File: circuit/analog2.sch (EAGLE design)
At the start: 44 parts, among them IC1 AD8532, IC2 74HC4052D, IC3 AD8532, IC4 4066D, IC5 4066D

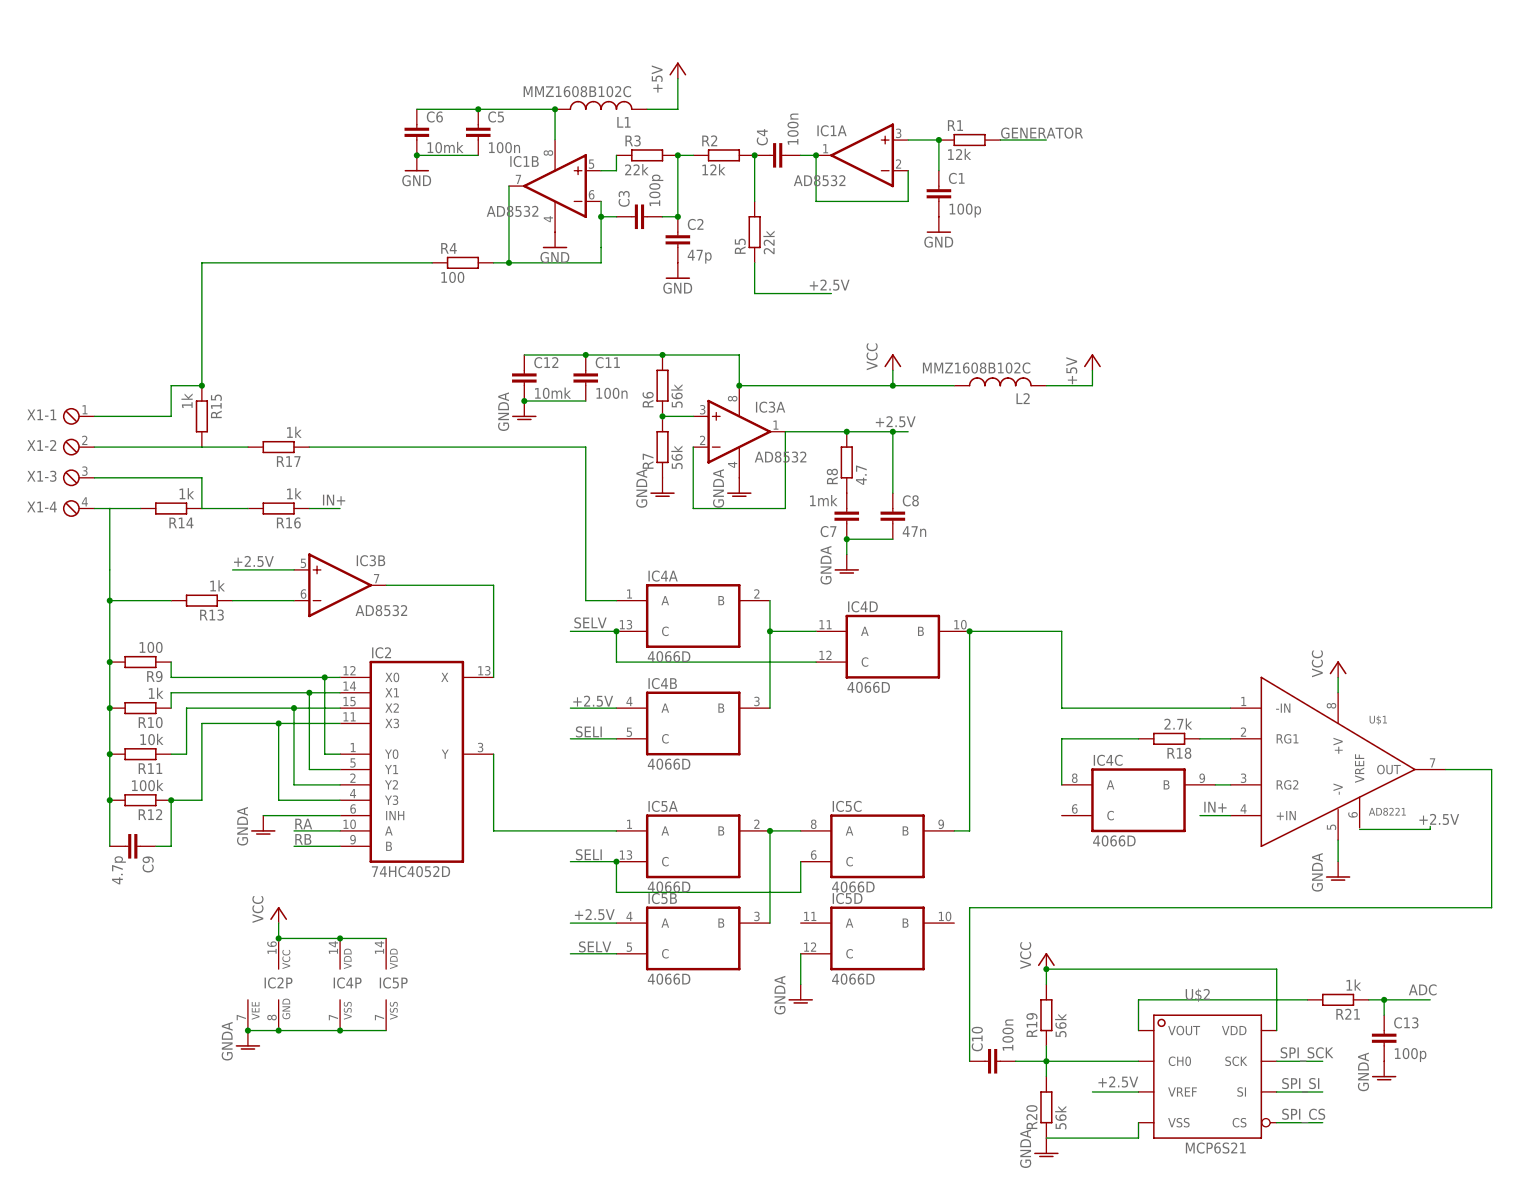
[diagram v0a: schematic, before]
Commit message: - analog to dual ADC STM32F103
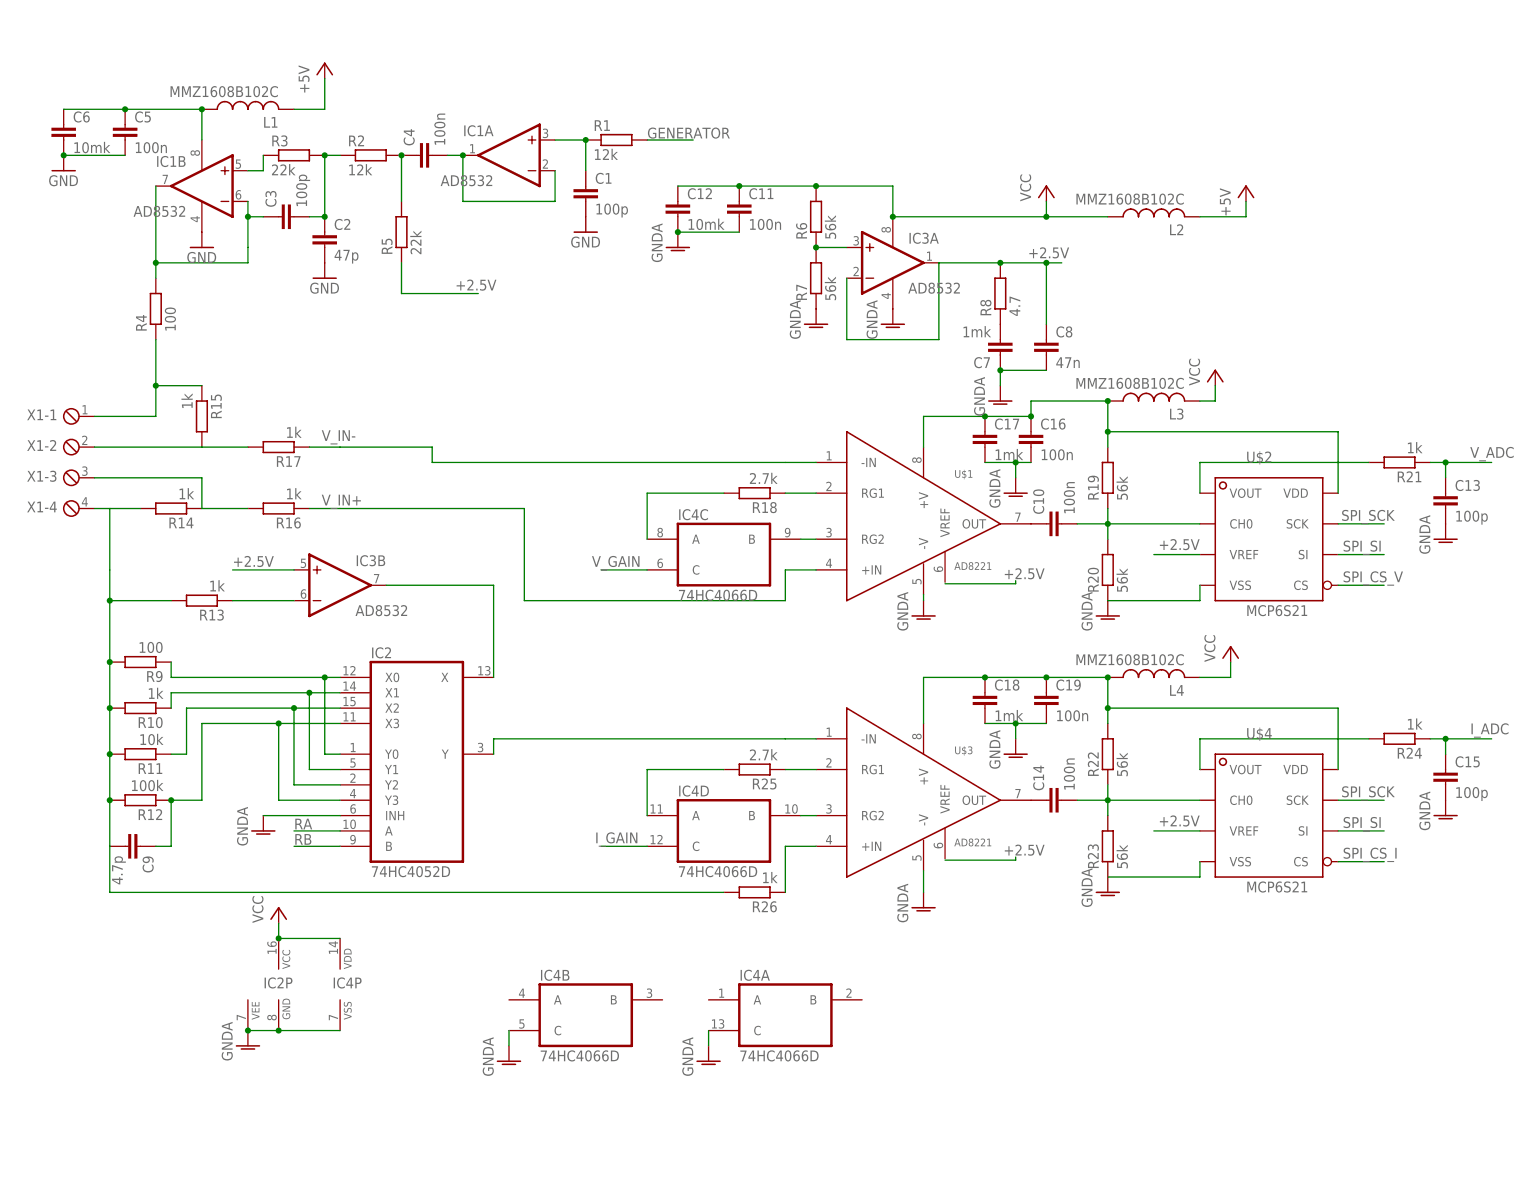
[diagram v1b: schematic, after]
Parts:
- removed IC5: 4066D, 40xx:4066D
- added C14, C16, C19: 100n, rcl:C-EUC0603
- added C15: 100p, rcl:C-EUC0805
- added C17, C18: 1mk, rcl:C-EUC0603
- added L3, L4: MMZ1608B102C, rcl:L-US
- added R22, R23: 56k, rcl:R-EU_R0805
- added R24, R26: 1k, rcl:R-EU_R0805
- added R25: 2.7k, rcl:R-EU_R0805
- added U$3: AD8221, balmer:AD8221
- added U$4: MCP6S21, balmer:MCP6S21
- IC4: value 4066D -> 74HC4066D
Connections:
- net ADC renamed V_ADC
- net IN+ renamed V_IN+
- net SPI_CS renamed SPI_CS_V
- removed net N$20 (its old number): IC4A.A, R17.1
- removed net SELI: IC4B.C, IC5A.C, IC5C.C
- removed net SELV: IC4A.C, IC4D.C, IC5B.C
- new net I_ADC: C15.1, R24.1
- new net I_GAIN: IC4D.C
- new net I_IN+: R26.1, U$3.+IN
- new net I_IN-: IC2A.Y, U$3.-IN
- new net N$26: R24.2, U$4.VOUT
- new net N$31: IC4D.A, R25.2
- new net N$32: C16.1, C17.1, L3.1, R19.2, U$1.+V, U$2.VDD
- new net N$34: C18.1, C19.1, L4.1, R22.2, U$3.+V, U$4.VDD
- new net SPI_CS_I: U$4.CS
- new net V_GAIN: IC4C.C
- new net V_IN-: R17.1, U$1.-IN
- net +2.5V: now also U$4.VREF; no longer IC4B.A, IC5B.A
- net GNDA: now also C15.2, C16.2, C17.2, C18.2, C19.2, IC4A.C, IC4B.C, R23.1, U$3.-V, U$4.VSS; no longer IC5D.C, IC5P.VSS
- net N$18: now also R26.2
- net N$21: now also IC4D.B, U$3.RG2; no longer IC4A.B, IC4B.B, IC4D.A
- net N$22: now also R25.1, U$3.RG1; no longer IC5A.B, IC5B.B, IC5C.A
- net N$25: now also C14.2, R22.1, R23.2, U$4.CH0; no longer IC4D.B, IC5C.B, U$1.-IN
- net N$29: now also C14.1, U$3.OUT; no longer IC2A.Y, IC5A.A
- net SPI_SCK: now also U$4.SCK
- net SPI_SI: now also U$4.SI
- net VCC: now also L3.2, L4.2; no longer IC5P.VDD, R19.2, U$1.+V, U$2.VDD
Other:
- moved on the sheet: C1, C10, C11, C12, C13, C2, C3, C4, C5, C6, C7, C8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

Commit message: - будем полностью перерисовывать под другие усилители , AD8532 имеет слишком высокий Input offset voltage.
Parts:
- added C20: 100n, rcl:C-EUC0603
- added X2, X3, X4, X5, X6, X7, X8: (no value), con-phoenix-254:MPT2
- R1: device rcl:R-EU_R0805 -> rcl:R-EU_R1206
- R21: device rcl:R-EU_R0805 -> rcl:R-EU_R1206W
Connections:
- net +5V: now also X2-1.1
- net GENERATOR: now also X8-1.1
- net GND: no longer C1.2, C2.2, IC1P.V-
- net GNDA: now also C1.2, C2.2, C20.1, IC1P.V-, X2-2.1
- net I_ADC: now also X5-2.1
- net I_GAIN: now also X3-2.1
- net N$9: now also C20.2
- net RA: now also X4-1.1
- net RB: now also X4-2.1
- net SPI_CS_I: now also X7-2.1
- net SPI_CS_V: now also X7-1.1
- net SPI_SCK: now also X6-1.1
- net SPI_SI: now also X6-2.1
- net V_ADC: now also X5-1.1
- net V_GAIN: now also X3-1.1

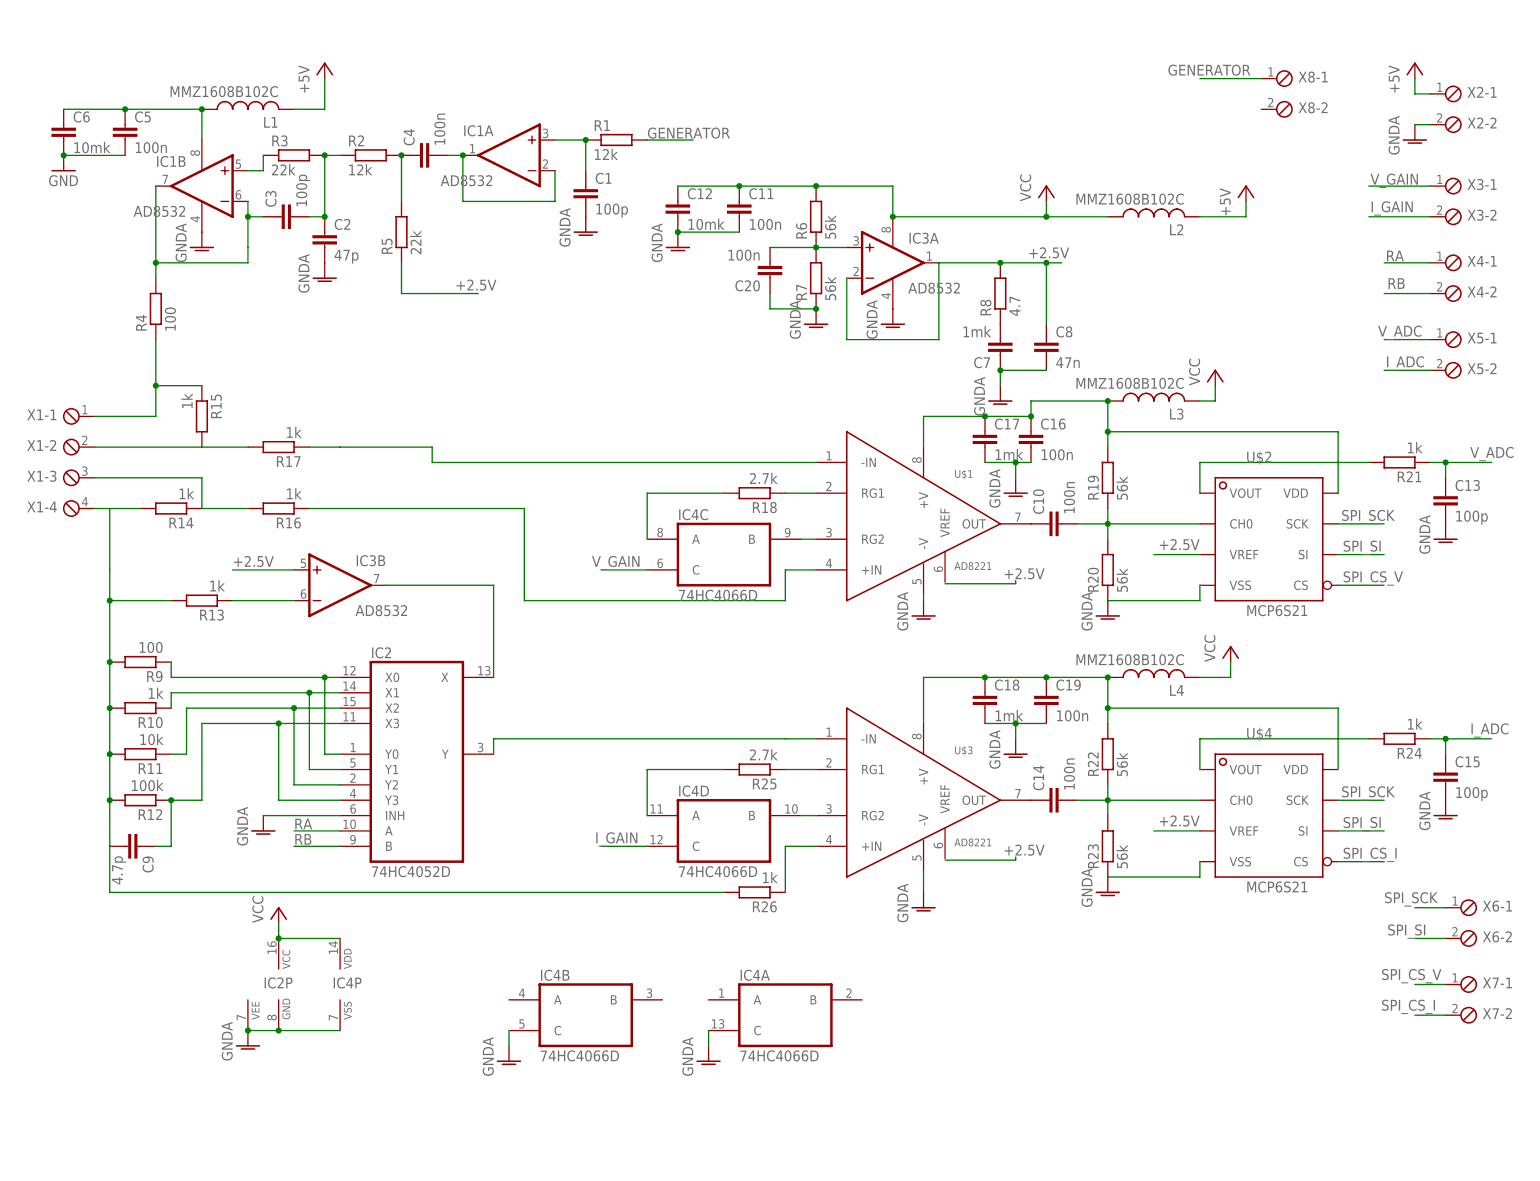
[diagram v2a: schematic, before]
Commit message: - AD825,  OP07C используем как усилители
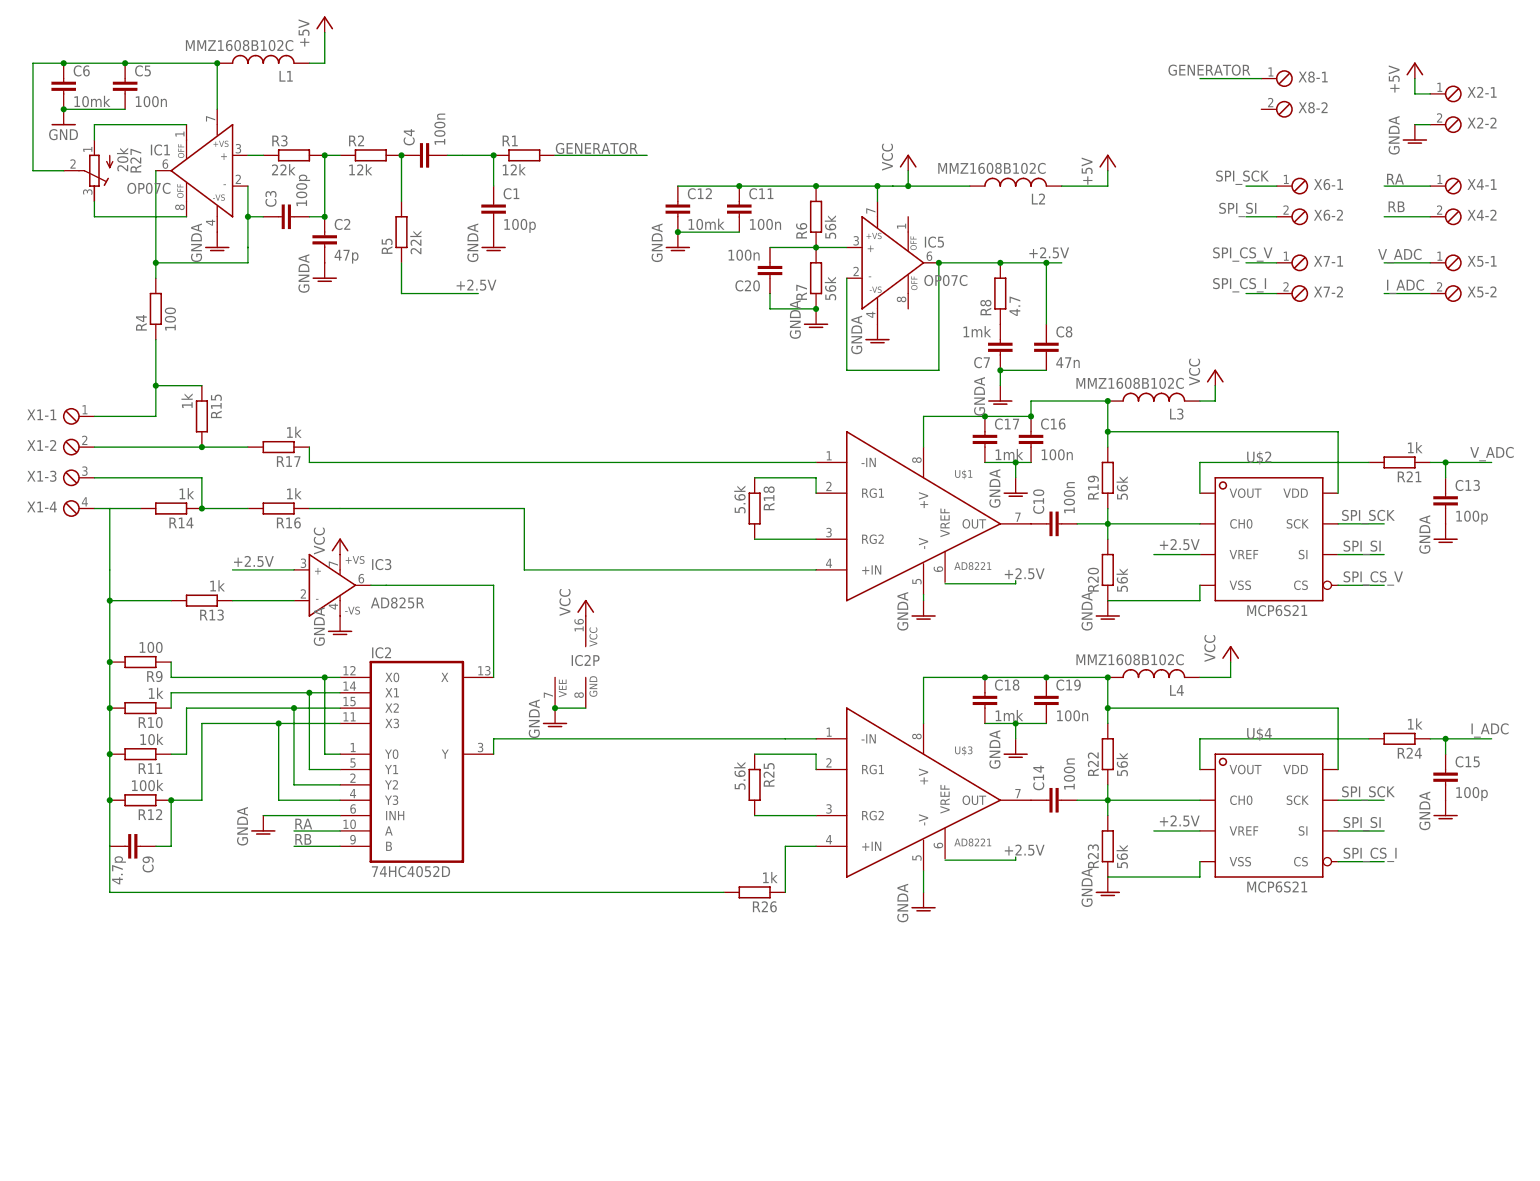
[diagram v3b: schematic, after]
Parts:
- removed IC4: 74HC4066D, 40xx:4066D
- removed X3: (no value), con-phoenix-254:MPT2
- added IC5: OP07C, analog-devices:AD817
- added R27: 20k, resistor:R-TRIMM64W
- IC1: value AD8532 -> OP07C; device linear:LM358D -> analog-devices:AD817
- IC3: value AD8532 -> AD825R; device linear:LM358D -> analog-devices:AD825R
- R18, R25: value 2.7k -> 5.6k
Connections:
- net V_IN- renamed N$30
- removed net I_GAIN: IC4D.C, X3-2.1
- removed net N$30 (its old number): IC4C.A, R18.2
- removed net N$31: IC4D.A, R25.2
- removed net V_GAIN: IC4C.C, X3-1.1
- new net N$33: IC1.OFF@2, R27.A
- new net N$35: IC1.OFF@1, R27.E
- net +2.5V: now also IC3.IN+, IC5.IN-, IC5.OUT; no longer IC3A.-IN, IC3A.OUT, IC3B.+IN
- net GNDA: now also IC1.-VS, IC3.-VS, IC5.-VS; no longer IC1P.V-, IC3P.V-, IC4A.C, IC4B.C, IC4P.VSS
- net N$1: no longer IC1A.-IN, IC1A.OUT
- net N$11: now also IC3.OUT; no longer IC3B.OUT
- net N$2: no longer IC1A.+IN
- net N$21: now also R25.2; no longer IC4D.B
- net N$23: now also R18.2; no longer IC4C.B
- net N$5: now also IC1.IN-, IC1.OUT; no longer IC1B.-IN, IC1B.OUT
- net N$6: now also IC1.IN+; no longer IC1B.+IN
- net N$7: now also IC1.+VS, R27.S; no longer IC1P.V+
- net N$8: now also IC3.IN-; no longer IC3B.-IN
- net N$9: now also IC5.IN+; no longer IC3A.+IN
- net VCC: now also IC3.+VS, IC5.+VS; no longer IC3P.V+, IC4P.VDD
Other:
- moved on the sheet: C1, C5, C6, IC2P, L1, L2, R1, R18, R25, X4-1, X4-2, X5-1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

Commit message: - начали разводить плату
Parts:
- removed IC5: OP07C, analog-devices:AD817
- removed R27: 20k, resistor:R-TRIMM64W
- added C21: 1mk, rcl:C-EUC0603
- C3: device rcl:C-EUC0805 -> rcl:C-EUC1206
- C7: value 1mk -> 10mk; device rcl:C-EUC0603 -> rcl:C-EUC0805
- C8: value 47n -> 100n; device rcl:C-EUC0805 -> rcl:C-EUC0603
- IC3: value AD825R -> OP07C; device analog-devices:AD825R -> analog-devices:AD817
- R1: device rcl:R-EU_R1206 -> rcl:R-EU_R0805
- R21: device rcl:R-EU_R1206W -> rcl:R-EU_R0805
- R6, R7: value 56k -> 10k
- R8: value 4.7 -> 22k
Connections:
- removed net GND: C5.2, C6.2
- removed net N$1: C4.2
- removed net N$33: IC1.OFF@2, R27.A
- removed net N$35: IC1.OFF@1, R27.E
- removed net N$9: C20.2, IC5.IN+, R6.1, R7.2
- net +2.5V: now also C20.2, C7.1, R6.1, R7.2, R8.1; no longer C8.1, IC5.IN-, IC5.OUT, R5.1, R8.2
- net GNDA: now also C21.2, C5.2, C6.2, C7.2; no longer C7.1, IC5.-VS
- net N$10: now also C21.1, C8.1, R5.1, R8.2; no longer C7.2, R8.1
- net N$2: now also C4.2
- net N$7: no longer R27.S
- net VCC: no longer IC5.+VS
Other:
- moved on the sheet: C7, C8, R16, R8
